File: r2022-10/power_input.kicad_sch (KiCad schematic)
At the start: 31 parts, among them J8 Conn_01x06, Q1 Si4435, U19 SE5120ST33

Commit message: rev3: overhaul nearly all parts to be from jlc pcba
Only the inductor left.  I've marked a few through hole parts as DNP, as
I can solder them by hand, and already have the parts in stock.  But
everything else goes to JLC for assembly, with every attempt made to
stick to only basic parts, or shared parts.  Beyond that, price and
stocking!
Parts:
- removed C?: C_Small, symbol Device:C_Small
- removed D12: BZT52B12, Diode_SMD:D_SOD-123, symbol Diode:BZT52Bxx
- removed R?: 56k, symbol Device:R_Small
- removed R?: 440, symbol Device:R_Small
- removed R?: 10k, Resistor_SMD:R_0603_1608Metric, symbol Device:R_Small
- removed R?: 40k, symbol Device:R_Small
- removed U?: SiC402ACD, symbol Regulator_Switching:SiC402ACD
- added C40: 1uF, Capacitor_SMD:C_0603_1608Metric, symbol Device:C_Small
- added R25, R27: DNP, Resistor_SMD:R_0603_1608Metric, symbol Device:R_Small
- added R26: 100k, Resistor_SMD:R_0603_1608Metric, symbol Device:R_Small
- added R28: 510k, Resistor_SMD:R_0603_1608Metric, symbol Device:R_Small
- added R?: 20k, Resistor_SMD:R_0603_1608Metric, symbol Device:R_Small
- added U18: SiC437AED, Package_DFN_QFN:Vishay_MLP-44L_4x4, symbol Regulator_Switching:SiC437AED
- C43, C47: footprint Capacitor_SMD:C_0603_1608Metric -> Capacitor_SMD:C_0805_2012Metric; MPN CL10A106KP8NNNC -> CL21A106KAYNNNE; lcsc# C19702 -> C15850
- C44, C45, C46, C48: value 10uF-up? -> 10uF; footprint Capacitor_SMD:C_0603_1608Metric -> Capacitor_SMD:C_0805_2012Metric; MPN CL10A106KP8NNNC -> CL21A106KAYNNNE; lcsc# C19702 -> C15850
- D11: DNP (none) -> 1; MPN (none) -> SMF24A; jlc-basic (none) -> 0; lcsc# (none) -> C169430
- D13, J8: DNP (none) -> 1
- Q1: value Si4435 -> HSM6115; MPN (none) -> HSM6115; jlc-basic (none) -> 0; lcsc# (none) -> C700986
- U19: value SE5120ST33 -> AMS1117-33; MPN SE5120ST33 -> AMS1117-33; jlc-basic (none) -> 1; lcsc# (none) -> C6186
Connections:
- net +5V: now also U18.18 (VOUT)
- net +VDC: now also R?.1, U18.1 (VIN), U18.19 (EN), U18.22 (VIN)
- net GND: now also C39.2, C40.2, R26.1, R28.1, U18.13 (PGND), U18.16 (AGND), U18.25 (AGND), U18.3 (PGND)
- net PolProtG: now also R?.2
- net SW: now also U18.5 (SW)
- net VDD: now also R25.2, R27.2, U18.15 (VDD)
- net boot: now also U18.23 (BOOT)
- net fb: now also U18.17 (FB)
- net phase: now also U18.24 (PHASE)
- new net: U18.10 (GL), U18.11 (GL), U18.28 (GL)
- new net MODE1: R27.1, R28.2, U18.21 (MODE1)
- new net MODE2: R25.1, R26.2, U18.20 (MODE2)
- new net VDRV: C40.1, U18.12 (VDRV)
- no-connect marks 0 -> 1
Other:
- note added: "It's suggested that 30V is too low for 24V reverse pol prot. Perhaps, DPAK? many big fat options there? NCE60P25K NCE60P50K NCE01P18K IRFR9024NTRPBF IRFR5410TRPBF IRFR5305TRPBF NCE40P70K WSF15P10"
- note added: "Lol, no, there's enough caps going around"
- note added: "Shame....... Put a SE5120ST33 here instead of the x1117 and you can kill the queiescent current"
- note added: "We want a low breakdown voltage here, "normal" 5V tvs diodes will protect too late Must breakdown at ~6V to even have a _chance_ This is bogus though, no part will be able to handle the current here, I think we should just drop this"
- note added: "We're just trying to avoid the V_{GS} 20V limit being hit while attempting to keep it "well on" This works fine..."
- note added: "ds says 2.2 and 4.7, diff places evb has 1u 1u is _great_ for bom"
- note added: "jumper to disable?"
- note added: "mode1: 100k for 500kHz, 200k for 750kHz, 500k for 1MHz mode2: 100k for OCP at 9.7A, 200k for OCP at 14A, 500k for OCP at 18A. Mode1 to ground: skip, to vdd:forced ccm Mode2 to ground: Softstart=3ms, to vdd, 6ms Conclusion: default SS 3ms, skip mode, 1MHz, OCP at 9.7A"
- note removed: "AP1509/XL1509 are "sexy" but just use a SOT223-standard linear. (but not xxx1117! too much power waste!)"
- note removed: "At 8V input, with our 1MHz Ton, Ton_vinmin = 625ns Iripple vinmin = 1.8A... so no big deal?"
- note removed: "ESR max = vripple / iripple target 3% ripple, = 150mV / 4 = ~40mOhm max ESR for caps."
- note removed: "Iz is 5mA, to be "12V" in spec, but Vr is 8V, with only 0.1uA, So for _this_ purpose, of preventing the Vgs limit of 20V being exceeded, a large resistor is fine. 15V, 200uA => 15k 24V, 200uA => 60k 10k is probably just fine..."
- note removed: "L = (Vin-Vout)*t_{ON} / Iripple I Ripple = ~40% of max, = ~4A. at 1Mhz, L = ~1uH at 750kHz, L = ~1.3uH at 500kHz, L = ~2uH"
- note removed: "Peak output for Cout Vpeak of 5.2 (allows 200mV on a 10A load dump, very severe, but still very ok for USB) Iripple max of 4, I out of 10 (way too high, but we're conservative here) implies only 72uF minimum output. with a VPeak of 5.1, we would need 144uF. So, 200uF and call it winning?"
- note removed: "R_{ILim} = 446 * I_{ILim} * (0.099 * (5V-VDD) + 1) VDD=5V nominally, So, for 10A, 440ohm?"
- note removed: "V_{LDO} = 750mV * (1 + (R1/R2)) For VDD=5V, R2=10k, implies, R1 = 56k"
- note removed: "Vin = 24V+10% Freq = V_{out}/(T_{on}*V_{in}) R_{ton} = 1 / (25pF * Freq) Goal, 1Mhz for smaller inductors? or maybe 500kHz for lower inductance at higher currents? start with 1MHz: Rton = 40k (Ton = 190ns) 750kHz = 53k (Ton = 252ns) 500kHz = 80k (Ton = 378ns)"
- note removed: "We want a low breakdown voltage here, "normal" 5V tvs diodes will protect too late Must breakdown at ~6V to even have a _chance_"
- note removed: "min 10uF using 22uF for BOM optimization"

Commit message: r3: add power good led, add auto switch 5v sources
copied from nanopi usb sections.

still need to adjust the spacing of the leds, and decide on ordering,
with or without eeprom permanently.
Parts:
- added D13: HS1B, LED_SMD:LED_0805_2012Metric, symbol Device:LED_Small
- added R30: 330, Resistor_SMD:R_0603_1608Metric, symbol Device:R_Small
- L1: footprint Inductor_SMD:L_AVX_LMLP07A7 -> Inductor_SMD:L_Chilisin_BMRx00060630; MPN LMLP07A7M1R5DTAS -> MHCI06030-1R5M-R8A; jlc-basic (none) -> 0; lcsc# (none) -> C329386; old_MPN (none) -> LMLP07A7M1R5DTAS
- gave numbers to parts that had none: 1
- renumbered C43 to C42, C47 to C43, C42 to C44, C44 to C45, C45 to C46, C46 to C47, D13 to D12, R24 to R23, R30 to R31, R31 to R34
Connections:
- net +5V: now also R30.2
- net pgood: now reaches U18.14 (PGOOD)
- net pgood: now also D13.1 (K)
- new net: D13.2 (A), R30.1
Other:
- moved on the sheet: C42, C43, U19

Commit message: r3: fix spaces in lcsc fields
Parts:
- C38, C41, C44: lcsc# C14663 -> C14663
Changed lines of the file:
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@@
       (effects (font (size 1.27 1.27)) hide)
     )
-    (property "lcsc#" " C14663 " (id 5) (at 223.52 119.38 0)
+    (property "lcsc#" "C14663" (id 5) (at 223.52 119.38 0)
       (effects (font (size 1.27 1.27)) hide)
     )
@@
       (effects (font (size 1.27 1.27)) hide)
     )
-    (property "lcsc#" " C14663" (id 5) (at 86.36 119.38 0)
+    (property "lcsc#" "C14663" (id 5) (at 86.36 119.38 0)
       (effects (font (size 1.27 1.27)) hide)
     )
@@
       (effects (font (size 1.27 1.27)) hide)
     )
-    (property "lcsc#" " C14663 " (id 5) (at 185.42 137.16 0)
-      (effects (font (size 1.27 1.27)) hide)
-    )
+    (property "lcsc#" "C14663" (id 5) (at 185.42 137.16 0)
+      (effects (font (size 1.27 1.27)) hide)
+    )

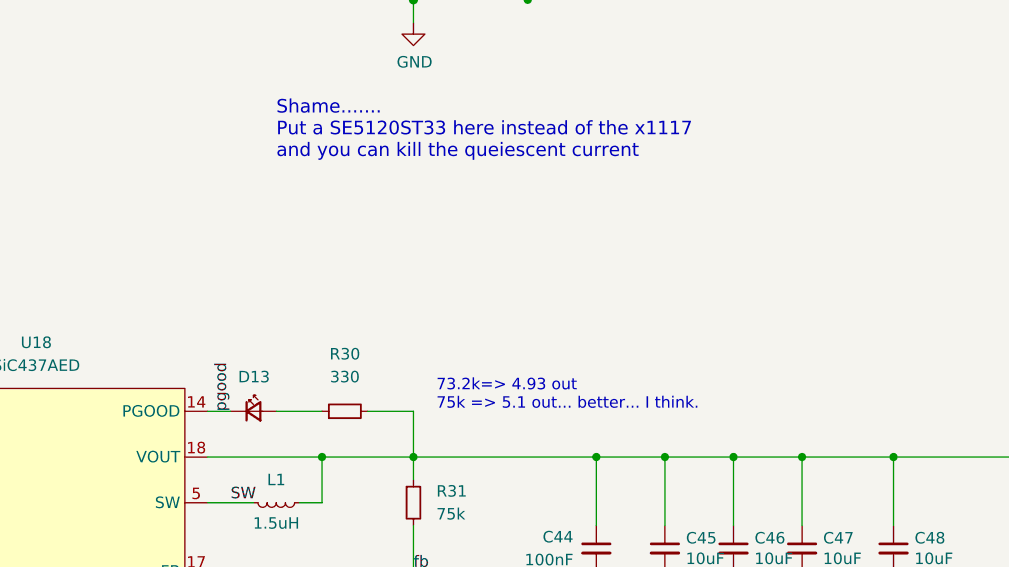
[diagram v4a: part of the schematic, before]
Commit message: rev3-2022-10: add fixme text on errors
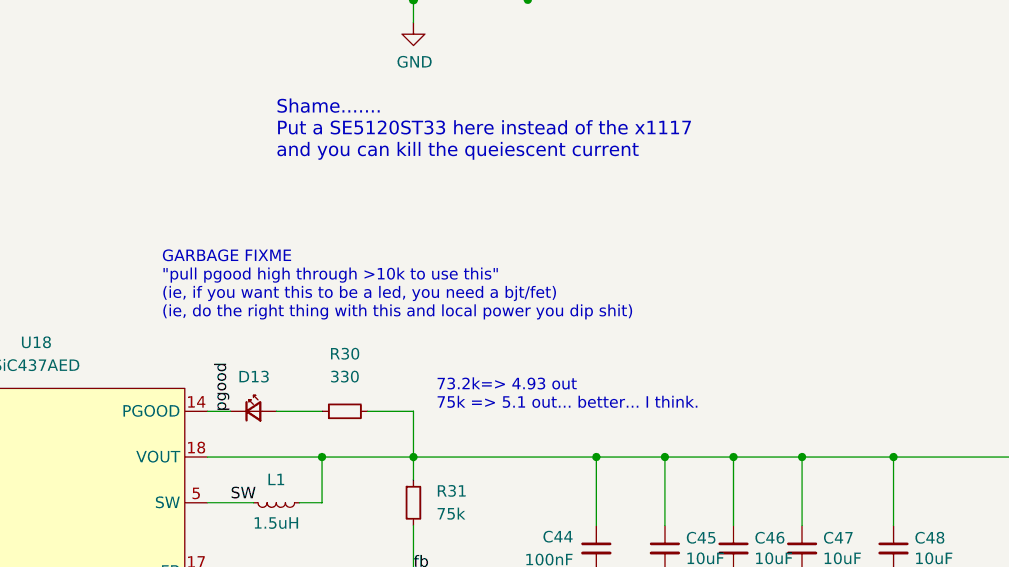
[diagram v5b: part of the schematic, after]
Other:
- note added: "GARBAGE FIXME "pull pgood high through >10k to use this" (ie, if you want this to be a led, you need a bjt/fet) (ie, do the right thing with this and local power you dip shit)"
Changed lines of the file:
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@@
+    (effects (font (size 1.27 1.27)) (justify left bottom))
+  )
+  (text "GARBAGE FIXME\n\"pull pgood high through >10k to use this\"\n(ie, if you want this to be a led, you need a bjt/fet)\n(ie, do the right thing with this and local power you dip shit)"
+    (at 175.26 93.98 0)
     (effects (font (size 1.27 1.27)) (justify left bottom))
   )
